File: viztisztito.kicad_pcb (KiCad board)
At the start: 2 copper layers, 71 parts, among them P1 WATER_LEVEL_CONN, P11 CONN_01X01, P13 CONN_01X01, P14 CONN_01X02, P15 FUSE, P2 BOARD_CONN, P4 CONN_01X03, P6 CONN_01X02, P9 CONN_01X10, Q1 BC850, T1 TRANSFO, U1 SPX2920M3-3.3, U10 ACS722, U2 LTV-847, U3 SHARPS202S02, U4 ACS716, U5 MCP3004, U6 TC77, U7 SPX2920M3-3.3, U8 SPX2920M3-3.3, U9 SPX2920M3-3.3

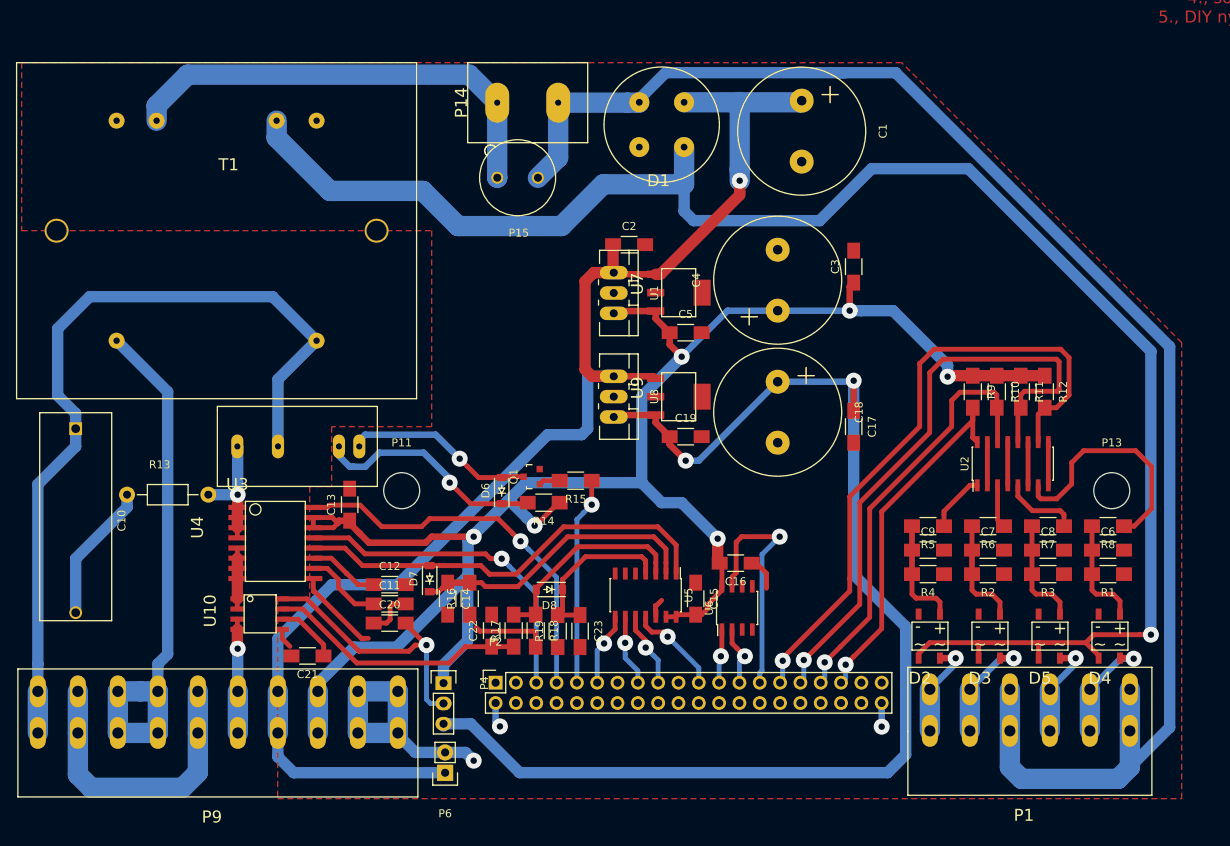
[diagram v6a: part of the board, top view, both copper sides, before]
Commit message: new layout, added psu
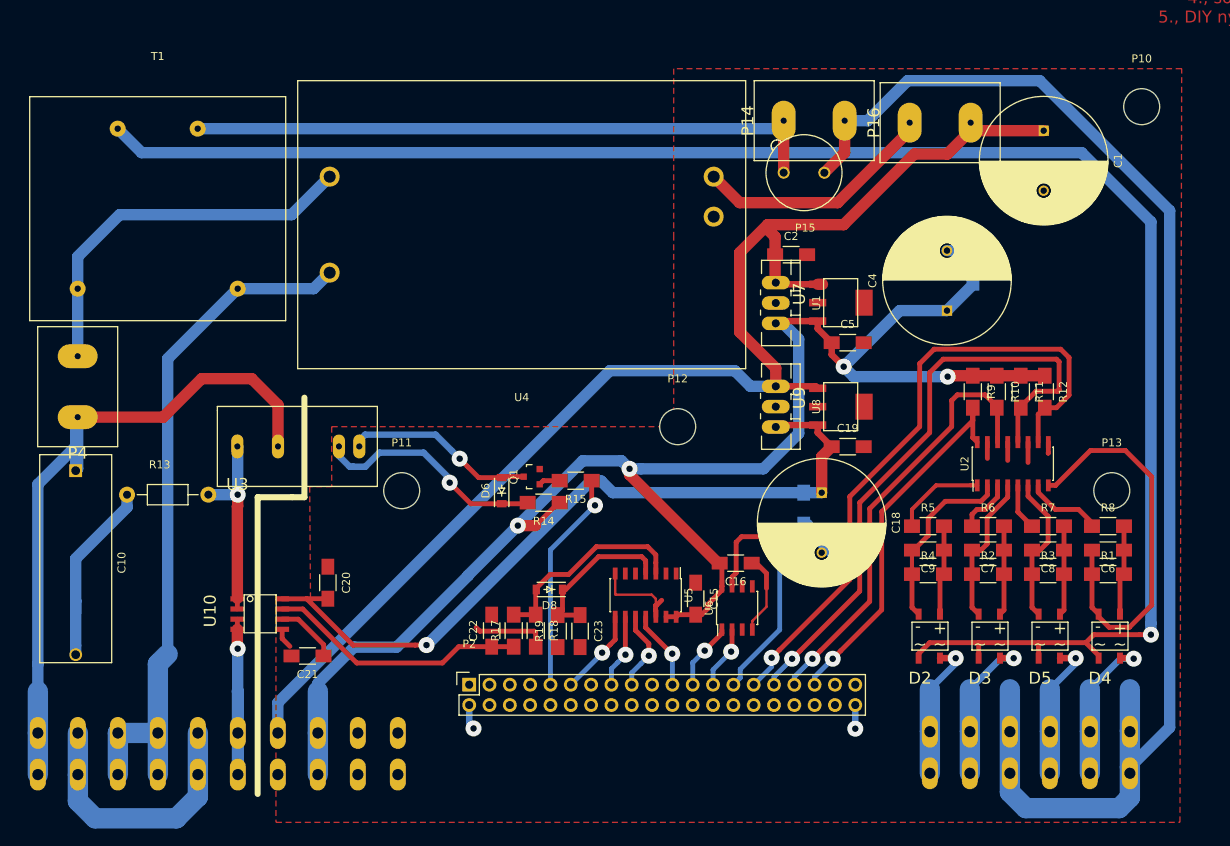
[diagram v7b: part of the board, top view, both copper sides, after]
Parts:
- removed C11, C12: 1nF, Capacitors_SMD:C_1206_HandSoldering
- removed C13, C14: 10uF, Capacitors_SMD:C_1206_HandSoldering
- removed D1: Diode_Bridge, libs:rb1a_mb6sbridge
- removed D7: D, Diodes_SMD:SOD-123
- removed P6: CONN_01X02, Pin_Headers:Pin_Header_Straight_1x02
- removed R16: 100k, Resistors_SMD:R_1206_HandSoldering
- added P10: CONN_01X01, Mounting_Holes:MountingHole_4-5mm, F.Cu at (158.0, 98.5)
- added P12: CONN_01X01, Mounting_Holes:MountingHole_4-5mm, F.Cu at (100.0, 138.5)
- added P16: CONN_01X02, libs:PIN_CONN_0.3Inch, F.Cu at (132.8, 100.5)
- C1: footprint Capacitors_Elko_ThroughHole:Elko_vert_31.5x16mm_RM7.5 -> Capacitors_ThroughHole:C_Radial_D16_L31.5_P7.5
- C17, C3, P1, P9: moved to B.Cu
- C18, C4: footprint Capacitors_Elko_ThroughHole:Elko_vert_31.5x16mm_RM7.5 -> Capacitors_ThroughHole:C_Radial_D16_L30_P7.5
- P4: value CONN_01X03 -> CONN_01X02; footprint Socket_Strips:Socket_Strip_Straight_1x03 -> libs:PIN_CONN_0.3Inch
- T1: footprint libs:MYRRA_44266 -> libs:MYRRA44050_IsolationTransformer
- U4: value ACS716 -> PCB_SWITCH_PSU; footprint libs:ACS716 -> libs:VTX_214_010_109_AC_DC_PCB_Mount_Power_Supply
- moved P4 58.9 mm to (25.0, 133.5), turned to 0 degrees
- moved U4 50.2 mm to (80.5, 113.2), turned to 0 degrees
- moved P14 35.9 mm to (117.1, 100.2)
- moved P15 35.8 mm to (115.8, 106.8)
- moved C1 30.5 mm to (145.8, 101.5)
- moved C4 21.2 mm to (133.7, 124.0)
- moved C19 20.3 mm to (121.2, 141.0)
- moved C2 20.3 mm to (114.2, 117.0)
- moved C5 20.3 mm to (121.2, 128.0)
- moved U1 20.3 mm to (112.3, 123.0)
- moved U7 20.3 mm to (117.5, 123.0)
- moved U8 20.3 mm to (112.3, 136.0)
- moved U9 20.3 mm to (117.5, 136.0)
- moved C18 14.9 mm to (118.0, 146.8)
- moved C3 14.9 mm to (136.9, 118.5)
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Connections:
- net RECT_VCC renamed 9V
- C20 pad 2: Net-(C20-Pad2) -> +5V
- C6 pad 2: GNDREF -> /water_level/GND4
- C7 pad 2: GNDREF -> /water_level/GND2
- C8 pad 2: GNDREF -> /water_level/GND3
- C9 pad 2: GNDREF -> /water_level/GND1
- D2 pad 1: GNDREF -> /water_level/GND1
- D3 pad 1: GNDREF -> /water_level/GND2
- D4 pad 1: GNDREF -> /water_level/GND4
- D5 pad 1: GNDREF -> /water_level/GND3
- P2 pad 5: /SSR_N_SENSING/!FAULT -> (no net)
- P2 pad 7: /SSR_N_SENSING/FAULT_EN -> (no net)
- P4 pad 1: +3V3 -> 230VPHASE
- P4 pad 2: Net-(C20-Pad2) -> 230VPHASE_AFTER
- R1 pad 1: GNDREF -> /water_level/GND4
- R13 pad 2: Net-(P7-Pad2) -> Net-(R13-Pad2)
- R2 pad 1: GNDREF -> /water_level/GND2
- R3 pad 1: GNDREF -> /water_level/GND3
- R4 pad 1: GNDREF -> /water_level/GND1
- T1 pad 1: 230VPHASE -> 230VPHASE_AFTER
- U10 pad 1: Net-(P7-Pad1) -> Net-(R13-Pad2)
- U10 pad 2: Net-(P7-Pad1) -> Net-(P8-Pad2)
- U10 pad 8: Net-(C20-Pad2) -> +5V
- U2 pad 2: GNDREF -> /water_level/GND1
- U2 pad 4: GNDREF -> /water_level/GND2
- U2 pad 6: GNDREF -> /water_level/GND3
- U2 pad 8: GNDREF -> /water_level/GND4
- U3 pad 1: Net-(P7-Pad2) -> Net-(R13-Pad2)
- U4 pad 1: Net-(P7-Pad2) -> 230VPHASE_AFTER
- U4 pad 2: Net-(P7-Pad2) -> 230VNULL
- U4 pad 3: Net-(P7-Pad2) -> Net-(P16-Pad1)
- U4 pad 4: Net-(P7-Pad2) -> GNDREF
- U5 pad 1: /DIGITAL_COMM/ADCH0 -> (no net)
- U5 pad 2: /DIGITAL_COMM/ADCH1 -> (no net)
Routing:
- net +5V: track 152.4 -> 96.6 mm, vias 2 -> 1
- net /DIGITAL_COMM/ADCH0: track 53.7 -> 0.00 mm
- net /water_level/GND4: track 0.00 -> 49.1 mm
- net /SSR_N_SENSING/FAULT_EN: track 48.3 -> 0.00 mm, vias 1 -> 0
- net 230VPHASE_AFTER: track 0.00 -> 48.1 mm
- net /SSR_N_SENSING/!FAULT: track 41.9 -> 0.00 mm, vias 1 -> 0
- net GNDREF: track 95.3 -> 57.0 mm, vias 3 -> 2
- net /DIGITAL_COMM/ADCH1: track 37.4 -> 0.00 mm
- net Net-(C20-Pad2): track 33.9 -> 0.00 mm, vias 1 -> 0
- net Net-(P16-Pad1): track 0.00 -> 30.6 mm
- net +3V3: track 224.9 -> 194.6 mm, vias 6 -> 4
- net AC+: track 195.5 -> 171.4 mm
- net Net-(R13-Pad2): track 0.00 -> 24.0 mm, vias 0 -> 1
- net Net-(P14-Pad1): track 56.9 -> 80.2 mm
- net /water_level/GND1: track 0.00 -> 23.1 mm
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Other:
- net class Default: clearance 0.635 -> 0.4064
- rule trace_clearance: 0.635 -> 0.4064
- board text removed: "hiba!!! GND"

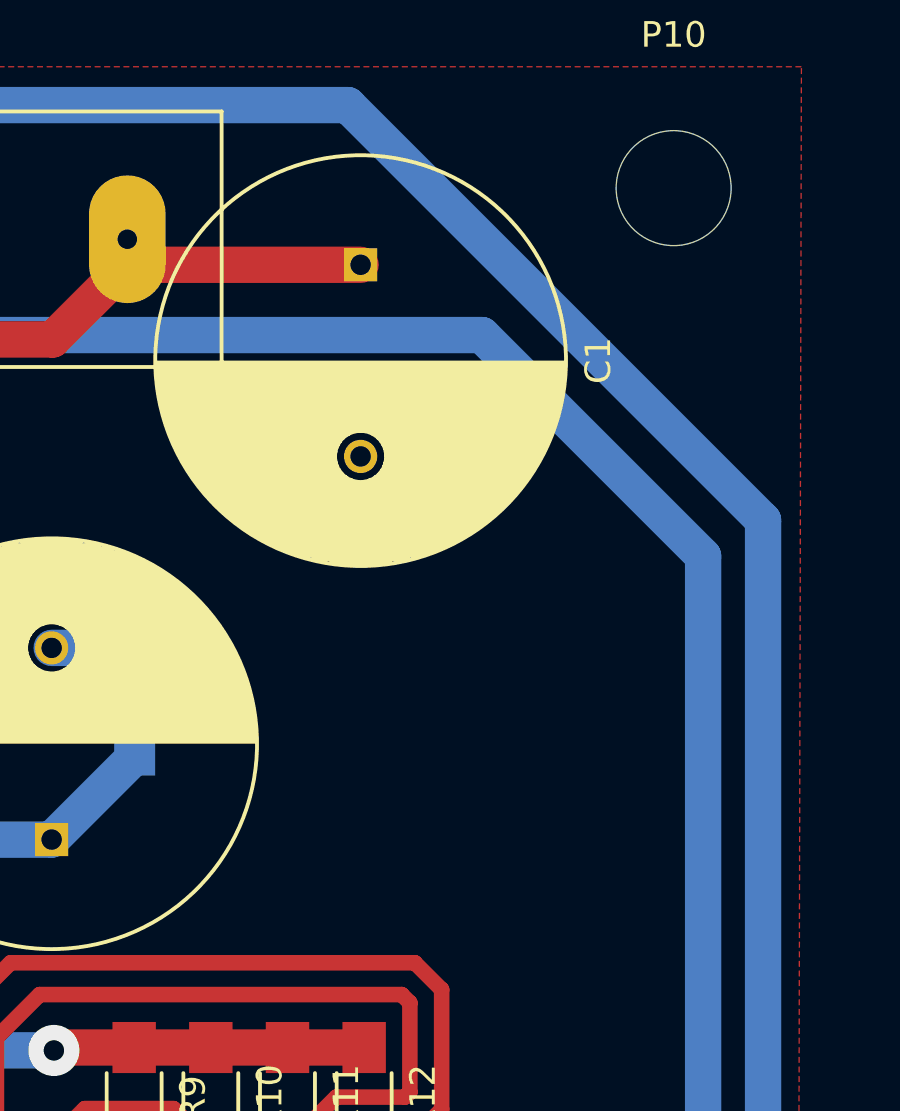
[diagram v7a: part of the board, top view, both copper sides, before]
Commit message: small change in a cap
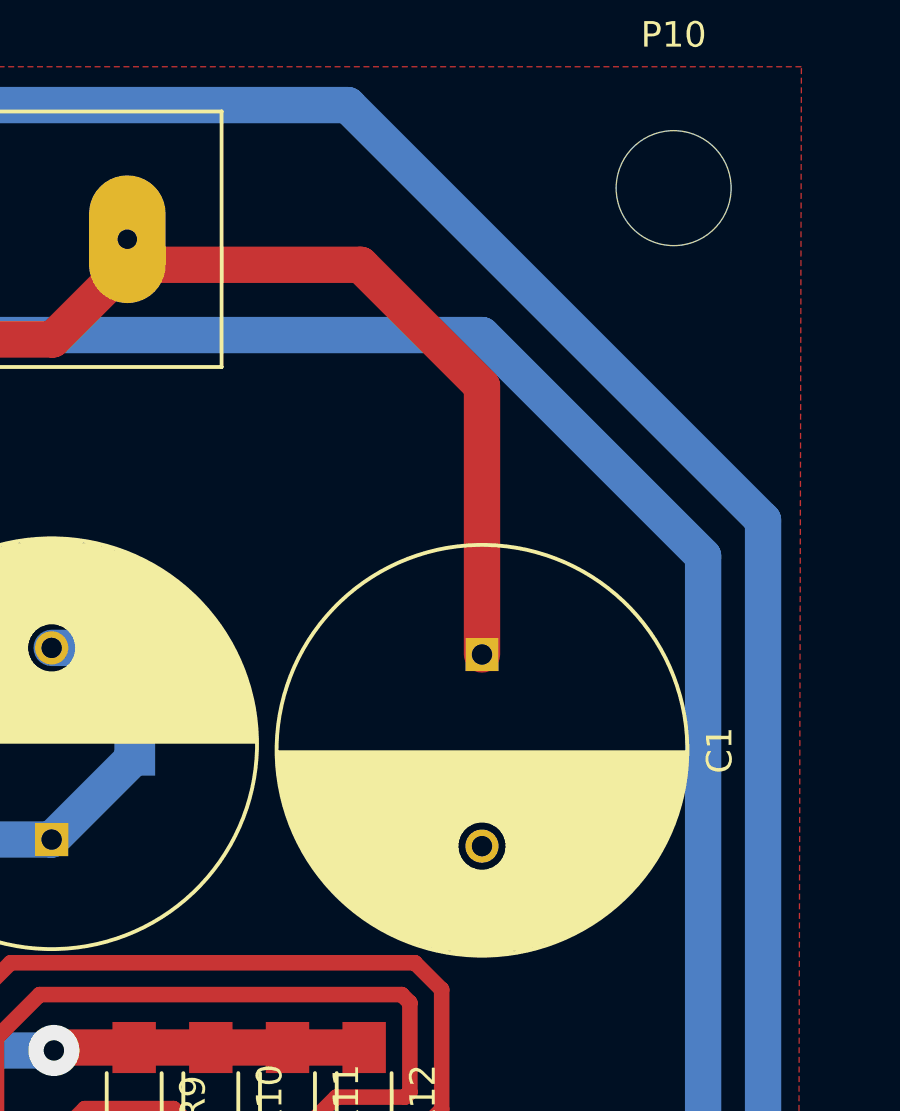
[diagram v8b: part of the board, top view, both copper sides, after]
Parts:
- moved C1 16.0 mm to (150.5, 116.8)
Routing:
- net 9V: track 167.3 -> 184.5 mm
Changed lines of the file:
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@@
     (thickness 1.6)
     (drawings 5)
-    (tracks 515)
+    (tracks 517)
     (zones 0)
     (modules 66)
@@
   )
   (setup
-    (last_trace_width 0.3048)
+    (last_trace_width 1.4224)
     (user_trace_width 0.254)
     (user_trace_width 0.3048)
@@
   )
   (module Capacitors_ThroughHole:C_Radial_D16_L31.5_P7.5 (layer F.Cu)
-    (at 145.75 101.5 270)
+    (at 150.5 116.75 270)
     (descr "Radial Electrolytic Capacitor Diameter 16mm x Length 31.5mm, Pitch 7.5mm")
     (tags "Electrolytic Capacitor")
@@
   (segment (start 107.75 110.5) (end 120 110.5) (width 1.4224) (layer F.Cu) (net 49))
   (segment (start 129 101.5) (end 129 100.5) (width 1.4224) (layer F.Cu) (net 49))
+  (segment (start 150.5 116.75) (end 150.5 106.25) (width 1.4224) (layer F.Cu) (net 50))
+  (segment (start 150.5 106.25) (end 145.75 101.5) (width 1.4224) (layer F.Cu) (net 50))
   (segment (start 50.024 176.784) (end 50.024 172.997673) (width 1.4224) (layer B.Cu) (net 50))
   (segment (start 50.024 172.997673) (end 91.521673 131.5) (width 1.4224) (layer B.Cu) (net 50))
